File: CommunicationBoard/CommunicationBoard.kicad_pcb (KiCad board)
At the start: 2 copper layers, 50 x 50 mm, 12 parts, among them P12 CONN_01X04, P4 CONN_01X07, P7 CONN_01X07, P9 CONN_01X04, U2 RFM95W-868S2

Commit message: Update PCB with Schematic
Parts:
- renumbered P7 to P1, P12 to P2, P9 to P3
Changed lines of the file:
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@@
-(kicad_pcb (version 4) (host pcbnew 4.0.0-rc1-stable)
+(kicad_pcb (version 4) (host pcbnew 4.0.3-stable)
   (general
     (links 29)
     (no_connects 1)
-    (area 65.222241 55.848816 178.060308 118.850001)
+    (area 88.524999 62.074999 138.675001 112.225001)
     (thickness 1.6)
     (drawings 25)
@@
       (effects (font (size 0.77216 0.77216) (thickness 0.138988)) (justify left bottom))
     )
-    (fp_text value RFM95W-868S2 (at -7.55 9.95) (layer F.SilkS)
+    (fp_text value RFM95W-868S2 (at -4.35 9.55) (layer F.SilkS)
       (effects (font (size 1 1) (thickness 0.15)) (justify left bottom))
     )
@@
     (descr "Through hole pin header")
     (tags "pin header")
-    (fp_text reference P4 (at 0.2 -3) (layer F.SilkS)
+    (fp_text reference P4 (at 2.4 16.4) (layer F.SilkS)
       (effects (font (size 1 1) (thickness 0.15)))
     )
@@
     (descr "Through hole pin header")
     (tags "pin header")
-    (fp_text reference P7 (at 0.15 -2.85 90) (layer F.SilkS)
+    (fp_text reference P1 (at 0.15 -2.85 90) (layer F.SilkS)
       (effects (font (size 1 1) (thickness 0.15)))
     )
@@
     (descr "Through hole pin header")
     (tags "pin header")
-    (fp_text reference P9 (at -0.25 -2.63 270) (layer F.SilkS)
+    (fp_text reference P3 (at -0.25 -2.63 270) (layer F.SilkS)
       (effects (font (size 1 1) (thickness 0.15)))
     )
@@
     (descr "Through hole pin header")
     (tags "pin header")
-    (fp_text reference P12 (at 0 -2.5) (layer F.SilkS)
+    (fp_text reference P2 (at 0 -2.5) (layer F.SilkS)
       (effects (font (size 1 1) (thickness 0.15)))
     )
@@
     (descr "Resistor, Axial,  RM 7.62mm, 1/3W,")
     (tags "Resistor Axial RM 7.62mm 1/3W R3")
-    (fp_text reference R1 (at 8.47 2 180) (layer F.SilkS)
-      (effects (font (size 1 1) (thickness 0.15)))
-    )
+    (fp_text reference R1 (at 6.07 2.2 180) (layer F.SilkS)
+      (effects (font (size 1 1) (thickness 0.15)))
+    )

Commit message: Update PCB via GPS & Telecomm board
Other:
- board text added: "GPS & Telecomm Board"
- board text removed: "Telemetry & GPS Board"
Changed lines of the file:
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@@
     (links 29)
     (no_connects 1)
-    (area 88.524999 62.074999 138.675001 112.225001)
+    (area 65.372241 55.998816 158.628572 118.850001)
     (thickness 1.6)
     (drawings 25)
@@
   )
   (layers
-    (0 F.Cu signal hide)
-    (31 B.Cu signal hide)
+    (0 F.Cu signal)
+    (31 B.Cu signal)
     (32 B.Adhes user)
     (33 F.Adhes user)
@@
       (effects (font (size 1 1) (thickness 0.15)))
     )
-    (fp_text value R (at 3.81 3.81 180) (layer F.Fab)
+    (fp_text value R (at 3.72 0.6 180) (layer F.Fab)
       (effects (font (size 1 1) (thickness 0.15)))
     )
@@
       (effects (font (size 1 1) (thickness 0.15)))
     )
-    (fp_text value R (at 3.81 3.81) (layer F.Fab)
+    (fp_text value R (at 3.375 -0.05) (layer F.Fab)
       (effects (font (size 1 1) (thickness 0.15)))
     )
@@
     (fp_line (start -1.99898 -23.50008) (end -1.09982 -21.20138) (layer B.SilkS) (width 0.15))
   )
-  (gr_text "Telemetry & GPS Board" (at 111.6 70) (layer B.SilkS)
+  (gr_text "GPS & Telecomm Board" (at 111.6 70) (layer B.SilkS)
     (effects (font (size 1.5 1.5) (thickness 0.3)) (justify mirror))
   )
@@
   (segment (start 112.6 74.61) (end 113.35 74.61) (width 0.5) (layer F.Cu) (net 2))
   (segment (start 113.35 74.61) (end 113.66 74.3) (width 0.5) (layer F.Cu) (net 2))
-  (segment (start 112.6 82.23) (end 115.07 82.23) (width 0.25) (layer F.Cu) (net 3))
-  (segment (start 115.07 82.23) (end 129.55 67.75) (width 0.25) (layer F.Cu) (net 3))
+  (segment (start 112.6 82.23) (end 115.07 82.23) (width 0.3) (layer F.Cu) (net 3))
+  (segment (start 115.07 82.23) (end 129.55 67.75) (width 0.3) (layer F.Cu) (net 3))
   (segment (start 129.55 67.75) (end 129.55 65.15) (width 0.25) (layer F.Cu) (net 3))
   (segment (start 129.55 65.3024) (end 129.55 65.15) (width 0.25) (layer F.Cu) (net 3))
-  (segment (start 112.6 79.69) (end 114.803533 79.69) (width 0.25) (layer F.Cu) (net 4))
+  (segment (start 112.6 79.69) (end 114.803533 79.69) (width 0.3) (layer F.Cu) (net 4))
   (segment (start 115.06 79.44) (end 115.053533 79.44) (width 0.25) (layer F.Cu) (net 4))
-  (segment (start 115.053533 79.44) (end 114.803533 79.69) (width 0.25) (layer F.Cu) (net 4))
-  (segment (start 115.06 79.44) (end 127.01 67.49) (width 0.25) (layer F.Cu) (net 4))
+  (segment (start 115.053533 79.44) (end 114.803533 79.69) (width 0.3) (layer F.Cu) (net 4))
+  (segment (start 115.06 79.44) (end 127.01 67.49) (width 0.3) (layer F.Cu) (net 4))
   (segment (start 127.01 67.49) (end 127.01 65.15) (width 0.25) (layer F.Cu) (net 4))
   (segment (start 127.01 65.3024) (end 127.01 65.15) (width 0.25) (layer F.Cu) (net 4))
@@
   (segment (start 92.866 95.48) (end 92.986 95.6) (width 0.25) (layer B.Cu) (net 21))
   (segment (start 91.6 98.02) (end 91.7524 98.02) (width 0.25) (layer F.Cu) (net 22))
-  (segment (start 91.7524 98.02) (end 97.1224 92.65) (width 0.25) (layer F.Cu) (net 22))
+  (segment (start 91.7524 98.02) (end 97.1224 92.65) (width 0.3) (layer F.Cu) (net 22))
   (segment (start 97.1224 92.65) (end 97.65 92.65) (width 0.25) (layer F.Cu) (net 22))
-  (segment (start 95.5 96.8124) (end 95.5 96.2) (width 0.25) (layer F.Cu) (net 23))
-  (segment (start 95.5 96.2) (end 97.05 94.65) (width 0.25) (layer F.Cu) (net 23))
+  (segment (start 95.5 96.8124) (end 95.5 96.2) (width 0.3) (layer F.Cu) (net 23))
+  (segment (start 95.5 96.2) (end 97.05 94.65) (width 0.3) (layer F.Cu) (net 23))
   (segment (start 97.05 94.65) (end 97.65 94.65) (width 0.25) (layer F.Cu) (net 23))
   (segment (start 91.6 100.56) (end 91.7524 100.56) (width 0.25) (layer F.Cu) (net 23))
-  (segment (start 91.7524 100.56) (end 95.5 96.8124) (width 0.25) (layer F.Cu) (net 23))
-  (segment (start 109.600511 108.900511) (end 99.35 98.65) (width 0.25) (layer F.Cu) (net 24))
-  (segment (start 99.35 98.65) (end 97.65 98.65) (width 0.25) (layer F.Cu) (net 24))
+  (segment (start 91.7524 100.56) (end 95.5 96.8124) (width 0.3) (layer F.Cu) (net 23))
+  (segment (start 109.600511 108.900511) (end 99.35 98.65) (width 0.3) (layer F.Cu) (net 24))
+  (segment (start 99.35 98.65) (end 97.65 98.65) (width 0.3) (layer F.Cu) (net 24))
   (segment (start 114.62 109.9) (end 113.620511 108.900511) (width 0.25) (layer F.Cu) (net 24))
-  (segment (start 113.620511 108.900511) (end 109.600511 108.900511) (width 0.25) (layer F.Cu) (net 24))
+  (segment (start 113.620511 108.900511) (end 109.600511 108.900511) (width 0.3) (layer F.Cu) (net 24))
   (segment (start 91.6 103.1) (end 91.7524 103.1) (width 0.25) (layer F.Cu) (net 24))
-  (segment (start 91.7524 103.1) (end 96.2024 98.65) (width 0.25) (layer F.Cu) (net 24))
-  (segment (start 96.2024 98.65) (end 97.65 98.65) (width 0.25) (layer F.Cu) (net 24))
-  (segment (start 95.85 110) (end 91.6 105.75) (width 0.25) (layer F.Cu) (net 25))
+  (segment (start 91.7524 103.1) (end 96.2024 98.65) (width 0.3) (layer F.Cu) (net 24))
+  (segment (start 96.2024 98.65) (end 97.65 98.65) (width 0.3) (layer F.Cu) (net 24))
+  (segment (start 95.85 110) (end 91.6 105.75) (width 0.3) (layer F.Cu) (net 25))
   (segment (start 91.6 105.75) (end 91.6 105.64) (width 0.25) (layer F.Cu) (net 25))
   (segment (start 91.6 105.64) (end 92.06 105.64) (width 0.25) (layer F.Cu) (net 25))
-  (segment (start 92.06 105.64) (end 97.05 100.65) (width 0.25) (layer F.Cu) (net 25))
+  (segment (start 92.06 105.64) (end 97.05 100.65) (width 0.3) (layer F.Cu) (net 25))
   (segment (start 97.05 100.65) (end 97.65 100.65) (width 0.25) (layer F.Cu) (net 25))
   (segment (start 120.96 82.04) (end 128.54 82.04) (width 0.5) (layer F.Cu) (net 31))

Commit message: Add label's Communication board
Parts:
- moved REF** 14.9 mm to (108.6, 74.6)
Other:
- board text added: "+BATT GND"
- board text added: "A1 A0"
- board text added: "A3 A2"
- board text added: "D6/DHT"
- board text added: "D8 D7"
- board text added: "GND +BATT"
- board text added: "INT1 INT0"
- board text added: "MOSI NSS"
- board text added: "RST"
- board text added: "SCK MISO"
- board text added: "SCL SDA"
- board text added: "S_RX S_TX"
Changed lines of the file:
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@@
     (links 29)
     (no_connects 1)
-    (area 65.372241 55.998816 158.628572 118.850001)
+    (area 88.524999 62.074999 138.675001 112.225001)
     (thickness 1.6)
-    (drawings 25)
+    (drawings 37)
     (tracks 101)
     (zones 0)
@@
   )
   (module Symbols:Symbol_OSHW-Logo_SilkScreen_BIG (layer B.Cu)
-    (at 107 59.8 180)
+    (at 108.625 74.575 180)
     (descr "Symbol, OSHW-Logo, Silk Screen, BIG")
     (tags "Symbol, OSHW-Logo, Silk Screen, BIG")
@@
     (fp_line (start -1.99898 -23.50008) (end -1.09982 -21.20138) (layer B.SilkS) (width 0.15))
   )
-  (gr_text "GPS & Telecomm Board" (at 111.6 70) (layer B.SilkS)
+  (gr_text "RST\n" (at 95.475 105.425) (layer B.SilkS)
     (effects (font (size 1.5 1.5) (thickness 0.3)) (justify mirror))
   )
+  (gr_text "MOSI\nNSS" (at 96 101.8) (layer B.SilkS)
+    (effects (font (size 1.5 1.5) (thickness 0.3)) (justify mirror))
+  )
+  (gr_text "SCK\nMISO\n" (at 96 96.825) (layer B.SilkS)
+    (effects (font (size 1.5 1.5) (thickness 0.3)) (justify mirror))
+  )
+  (gr_text "+BATT\n  GND" (at 96.975 91.875) (layer B.SilkS)
+    (effects (font (size 1.5 1.5) (thickness 0.3)) (justify mirror))
+  )
+  (gr_text D6/DHT (at 132.35 71.575 90) (layer B.SilkS)
+    (effects (font (size 1.5 1.5) (thickness 0.3)) (justify mirror))
+  )
+  (gr_text "S_RX\nS_TX" (at 128.475 69.675 90) (layer B.SilkS)
+    (effects (font (size 1.5 1.5) (thickness 0.3)) (justify mirror))
+  )
+  (gr_text "SCL\nSDA\n" (at 123.275 69.15 90) (layer B.SilkS)
+    (effects (font (size 1.5 1.5) (thickness 0.3)) (justify mirror))
+  )
+  (gr_text "GND\n +BATT\n" (at 118.15 69.375 90) (layer B.SilkS)
+    (effects (font (size 1.5 1.5) (thickness 0.3)) (justify mirror))
+  )
+  (gr_text "INT1\nINT0\n" (at 104.15 69.225 90) (layer B.SilkS)
+    (effects (font (size 1.5 1.5) (thickness 0.3)) (justify mirror))
+  )
+  (gr_text "D8\nD7\n" (at 98.675 68.375 90) (layer B.SilkS)
+    (effects (font (size 1.5 1.5) (thickness 0.3)) (justify mirror))
+  )
+  (gr_text "A1\nA0\n" (at 94.85 77.3) (layer B.SilkS)
+    (effects (font (size 1.5 1.5) (thickness 0.3)) (justify mirror))
+  )
+  (gr_text "A3\nA2\n" (at 94.925 72.4) (layer B.SilkS)
+    (effects (font (size 1.5 1.5) (thickness 0.3)) (justify mirror))
+  )
+  (gr_text "GPS & Telecomm Board" (at 110.06 84.99) (layer B.SilkS)
+    (effects (font (size 1.5 1.5) (thickness 0.3)) (justify mirror))
+  )

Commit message: Add 1.1v
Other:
- board text added: "CatSat 1.1v"
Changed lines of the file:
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@@
     (links 29)
     (no_connects 1)
-    (area 88.524999 62.074999 138.675001 112.225001)
+    (area 65.372241 55.998816 158.628572 118.850001)
     (thickness 1.6)
-    (drawings 37)
+    (drawings 38)
     (tracks 101)
     (zones 0)
@@
     (fp_line (start -1.99898 -23.50008) (end -1.09982 -21.20138) (layer B.SilkS) (width 0.15))
   )
+  (gr_text "CatSat 1.1v" (at 110.17 86.17) (layer B.SilkS)
+    (effects (font (size 1.5 1.5) (thickness 0.3)) (justify mirror))
+  )
   (gr_text "RST\n" (at 95.475 105.425) (layer B.SilkS)
     (effects (font (size 1.5 1.5) (thickness 0.3)) (justify mirror))
@@
     (effects (font (size 1.5 1.5) (thickness 0.3)) (justify mirror))
   )
-  (gr_text "GPS & Telecomm Board" (at 110.06 84.99) (layer B.SilkS)
+  (gr_text "GPS & Telecomm Board" (at 109.26 83.2) (layer B.SilkS)
     (effects (font (size 1.5 1.5) (thickness 0.3)) (justify mirror))
   )

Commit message: Fix Label Communication
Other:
- board text added: "BATT+ GND"
- board text added: "GND BATT+"
- board text removed: "+BATT GND"
- board text removed: "GND +BATT"
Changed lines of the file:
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@@
     (links 29)
     (no_connects 1)
-    (area 65.372241 55.998816 158.628572 118.850001)
+    (area 88.524999 62.074999 138.675001 112.225001)
     (thickness 1.6)
     (drawings 38)
@@
   )
   (layers
-    (0 F.Cu signal)
-    (31 B.Cu signal)
+    (0 F.Cu signal hide)
+    (31 B.Cu signal hide)
     (32 B.Adhes user)
     (33 F.Adhes user)
@@
     )
     (fp_text value ANT (at -0.06 -4.96 180) (layer F.SilkS)
-      (effects (font (size 1 1) (thickness 0.15)))
+      (effects (font (size 1 1) (thickness 0.25)))
     )
     (fp_line (start -1.2954 3.5052) (end 1.2954 3.5052) (layer F.SilkS) (width 0.1524))
@@
     (effects (font (size 1.5 1.5) (thickness 0.3)) (justify mirror))
   )
-  (gr_text "+BATT\n  GND" (at 96.975 91.875) (layer B.SilkS)
+  (gr_text "BATT+\nGND" (at 96 91.6) (layer B.SilkS)
     (effects (font (size 1.5 1.5) (thickness 0.3)) (justify mirror))
   )
@@
     (effects (font (size 1.5 1.5) (thickness 0.3)) (justify mirror))
   )
-  (gr_text "GND\n +BATT\n" (at 118.15 69.375 90) (layer B.SilkS)
+  (gr_text "GND\n BATT+" (at 118.15 69.375 90) (layer B.SilkS)
     (effects (font (size 1.5 1.5) (thickness 0.3)) (justify mirror))
   )

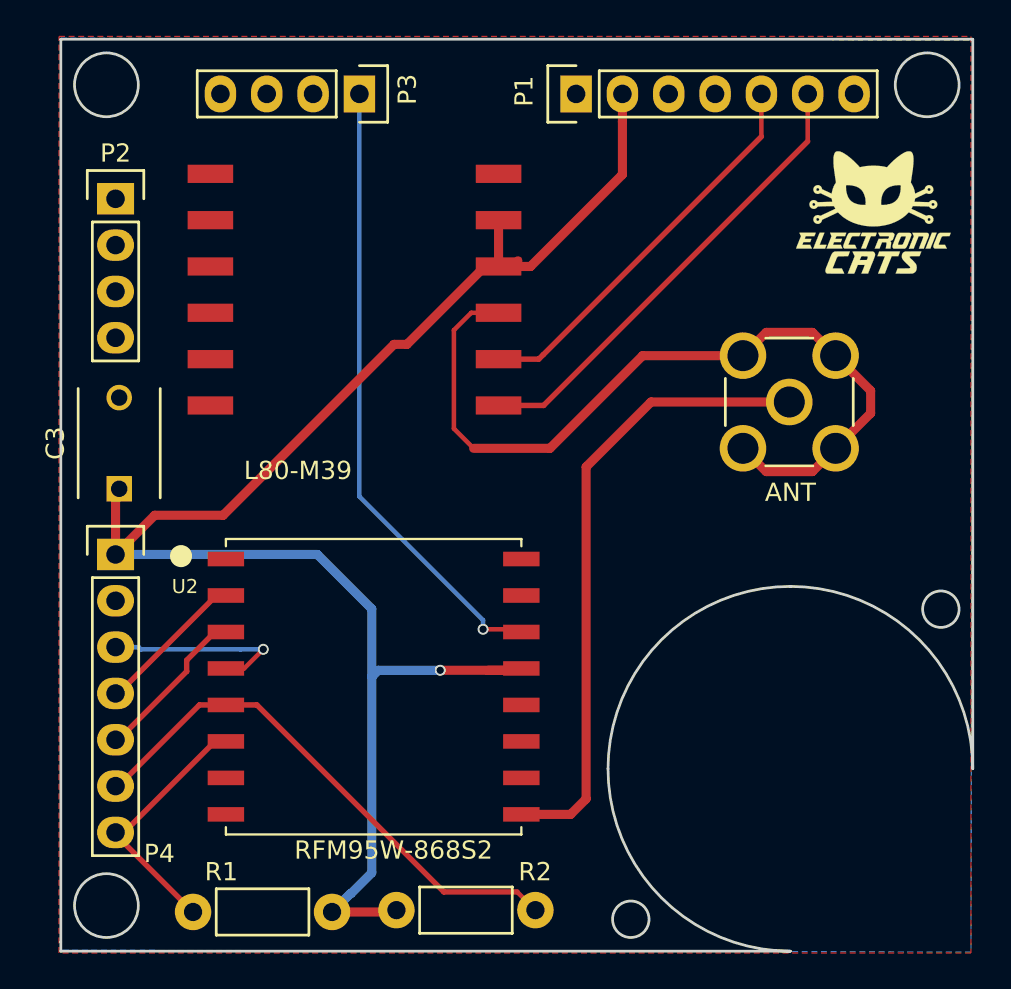
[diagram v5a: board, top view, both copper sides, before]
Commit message: Add larger holes
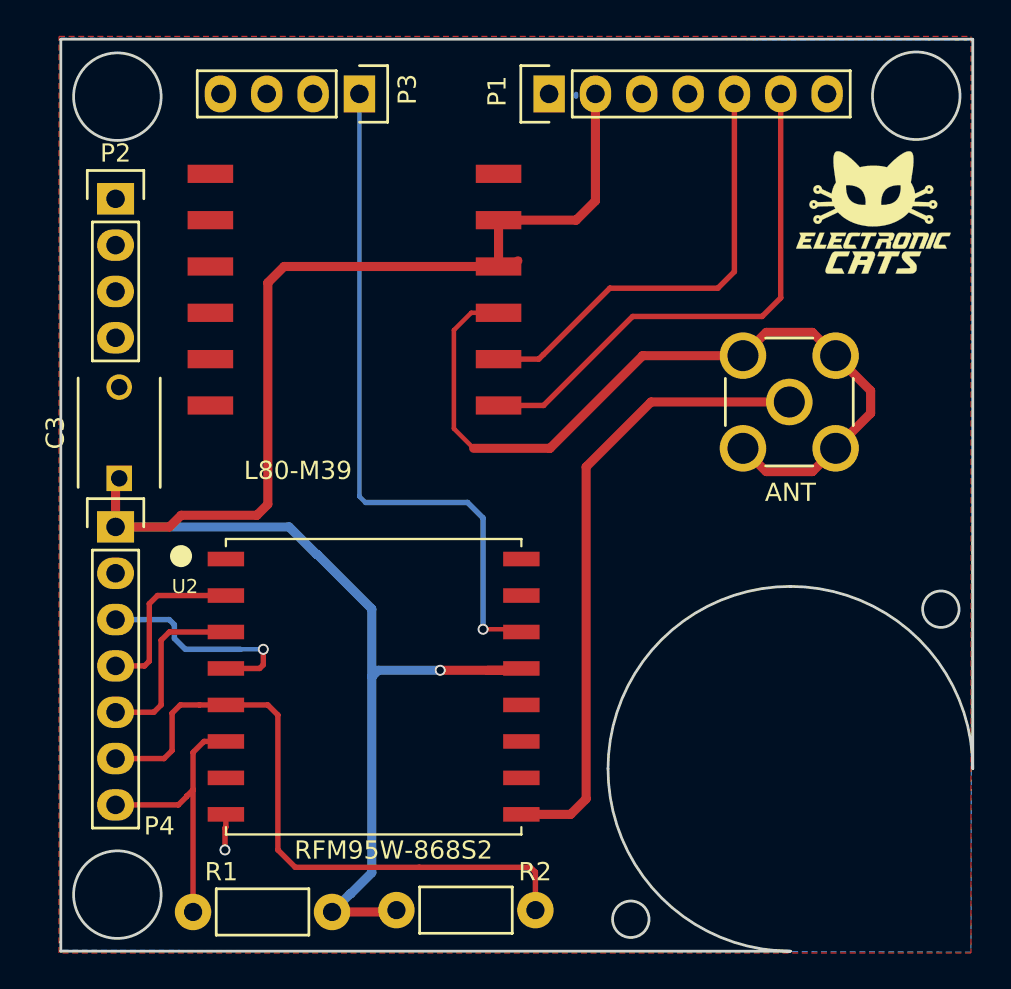
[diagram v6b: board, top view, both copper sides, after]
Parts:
- moved P4 1.51 mm to (91.6, 88.9)
- moved P1 1.48 mm to (115.4, 65.2)
- moved C3 0.58 mm to (91.8, 86.2)
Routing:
- net NSS: track 29.5 -> 35.7 mm
- net +BATT: track 94.8 -> 99.3 mm
- net S_TX: track 25.7 -> 29.1 mm
- net INT0: track 34.9 -> 38.2 mm
- net S_RX: track 22.0 -> 24.7 mm
- net GND: track 48.3 -> 50.1 mm, vias 0 -> 1
- net RST: track 14.2 -> 16.0 mm
- net MISO: track 8.27 -> 10.0 mm
- net MOSI: track 8.86 -> 10.6 mm
- net SCK: track 10.6 -> 12.2 mm
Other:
- outline, holes or cut-outs redrawn
- net class Default: trace_width 0.25 -> 0.3
